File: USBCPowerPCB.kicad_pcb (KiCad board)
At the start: 4 copper layers, 101 parts, among them IC2 TPS56A37RPAR, J1 USB_C_Receptacle_PowerOnly_6P, J10 GND_BANANA_OUT, J2 CC, J3 12V_OUT, J4 5V_ISOOUT, J5 5V_UNISOOUT, J6 12V_OUT_PIN, J7 5V_ISOOUT_PIN, J8 5V_UNISOOUT_PIN, J9 12V_BANANA_OUT, Q1 IRF9358TRPBF, Q2 BSL308PEH6327XTSA1, U1 TVS2200DRV, U2 CYPD3177-24LQXQT, U3 TPS562231DRLR, U4 TPS2116DRL, U5 TBA2-2411

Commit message: started routing
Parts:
- C11, C19, C9: footprint Capacitor_SMD:C_2220_5750Metric -> Capacitor_SMD:C_0805_2012Metric
- C14, NT1, R21, R23: moved to B.Cu
- C17, C18, C21, C22: footprint Capacitor_SMD:C_1210_3225Metric -> Capacitor_SMD:C_0805_2012Metric
- TP1, TP10, TP11, TP12, TP13, TP2, TP3, TP4, TP5, TP6, TP7, TP8, TP9: footprint TestPoint:TestPoint_Pad_D2.5mm -> TestPoint:TestPoint_Plated_Hole_D3.0mm
- moved J9 174.6 mm to (276.2, 113.1), turned to -90 degrees
- moved J10 154.3 mm to (259.9, 113.1), turned to -90 degrees
- moved L1 121.6 mm to (256.5, 100.5)
- moved C18 115.1 mm to (262.2, 107.8), turned to -90 degrees
- moved C9 111.8 mm to (243.0, 101.0), turned to -90 degrees
- moved C17 111.6 mm to (259.2, 107.8), turned to -90 degrees
- moved R24 111.3 mm to (248.6, 105.9), turned to 90 degrees
- moved C11 110.3 mm to (240.2, 101.0), turned to -90 degrees
- moved D9 108.9 mm to (237.5, 109.6), turned to 90 degrees
- moved C15 108.8 mm to (248.5, 96.8), turned to 90 degrees
- moved R25 106.2 mm to (242.9, 105.9), turned to -90 degrees
- moved C16 104.7 mm to (245.7, 106.0), turned to 90 degrees
- moved R23 104.4 mm to (242.9, 113.7), turned to -90 degrees
- moved R21 104.3 mm to (242.9, 110.0), turned to -90 degrees
- moved C14 103.0 mm to (245.6, 110.0), turned to -90 degrees
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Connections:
- net Net-(IC2-SW) renamed /12V Buck Converter/SW
- J4 pad 2: GNDPWR -> unconnected-(J4-Pin_2-Pad2)
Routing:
- net Net-(IC2-EN): track 0.00 -> 16.4 mm, vias 0 -> 1
- net Net-(IC2-MODE): track 0.00 -> 10.3 mm, vias 0 -> 1
- net GND: track 0.00 -> 8.94 mm, vias 0 -> 5
- net Net-(IC2-SS): track 0.00 -> 8.67 mm, vias 0 -> 1
- net /12V Buck Converter/FB: track 0.00 -> 8.16 mm
- net /VBUS: track 0.00 -> 6.09 mm
- net /12V Buck Converter/POWER_GOOD: track 0.00 -> 1.90 mm
- net GNDA: track 0.00 -> 1.17 mm, vias 0 -> 1
- added copper zone on F.Cu, net +12V
- added copper zone on F.Cu, net /12V Buck Converter/SW
- added copper zone on In2.Cu, net /VBUS
- added copper zone on B.Cu, net GND
- added copper zone on In1.Cu, net GND
- added copper zone on B.Cu, net GNDA
- added copper zone on In1.Cu, net GNDA

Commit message: more layout updates
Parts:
- moved C9 233.1 mm to (18.6, 38.1)
- moved C11 227.9 mm to (21.2, 38.1)
- moved C14 227.9 mm to (26.6, 47.0)
- moved C15 227.9 mm to (29.5, 33.9)
- moved C16 227.9 mm to (26.7, 43.0)
- moved C17 227.9 mm to (40.2, 44.9)
- moved C18 227.9 mm to (43.2, 44.9)
- moved D9 227.9 mm to (18.5, 46.7)
- moved IC2 227.9 mm to (28.1, 38.5)
- moved L1 227.9 mm to (37.5, 37.6)
- moved NT1 227.9 mm to (26.6, 52.1)
- moved R21 227.9 mm to (23.9, 47.0)
- moved R22 227.9 mm to (21.2, 43.0)
- moved R23 227.9 mm to (23.9, 50.7)
- moved R24 227.9 mm to (29.6, 43.0)
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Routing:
- net /12V Buck Converter/POWER_GOOD: track 1.90 -> 15.1 mm, vias 0 -> 2
- net GND: track 8.94 -> 18.9 mm, vias 5 -> 12
- net Net-(IC2-BOOT): track 0.00 -> 2.78 mm
- net Net-(IC2-MODE): track 10.3 -> 7.89 mm
- net Net-(IC2-EN): track 16.4 -> 16.9 mm, vias 1 -> 2
- added copper zone on In2.Cu, net +12V
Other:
- board outline added: 100 x 100 mm

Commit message: redid cypd layout, halfway through 12v buck layout
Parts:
- removed C10: 0.1uF, Capacitor_SMD:C_0805_2012Metric
- removed C13: 22uF, Capacitor_SMD:C_1210_3225Metric
- C14, NT1, R21, R23: moved to F.Cu
- J4: footprint UTSVT_Connectors:Molex_MicroFit3.0_1x2xP3.00mm_PolarizingPeg_Vertical -> UTSVT_Connectors:Molex_MicroFit3.0_1x4xP3.00mm_PolarizingPeg_Vertical
- L2: footprint UTSVT_Passive:INDPM110100X400N -> UTSVT_Passive:INDPM5452X300N
- R11, R13, R15, R17, R19, R20, R8: moved to B.Cu
- TP10, TP11, TP12, TP13: footprint TestPoint:TestPoint_Plated_Hole_D3.0mm -> TestPoint:TestPoint_THTPad_1.0x1.0mm_Drill0.5mm
- moved TP4 230.7 mm to (243.4, 90.1)
- moved J3 200.1 mm to (251.9, 60.2), turned to 0 degrees
- moved J6 198.7 mm to (249.1, 73.5), turned to 0 degrees
- moved TP1 177.7 mm to (237.3, 90.1)
- moved C9 140.4 mm to (130.5, 122.9), turned to 0 degrees
- moved R1 138.8 mm to (254.7, 88.5)
- moved R2 138.8 mm to (254.7, 91.5)
- moved R3 138.8 mm to (254.7, 94.4)
- moved R4 138.8 mm to (254.7, 97.4)
- moved R5 138.8 mm to (254.7, 100.3)
- moved R6 138.8 mm to (254.7, 103.3)
- moved C11 136.9 mm to (130.5, 120.6), turned to 0 degrees
- moved C12 133.3 mm to (130.5, 118.3), turned to 0 degrees
- moved R21 132.3 mm to (136.8, 116.0), turned to 0 degrees
- moved IC2 129.1 mm to (132.4, 114.6), turned to 180 degrees
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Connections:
- net Net-(U3-SW) renamed /5V Buck Converter/SW
- R26 pad 1: +3.3V -> +12V
- R31 pad 1: +5V -> /5V_BUCK
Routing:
- net /CC2: track 0.00 -> 26.3 mm, vias 0 -> 2
- net /CC1: track 0.00 -> 22.6 mm
- net /Power Delivery Controller/VBUS_MAX: track 0.00 -> 17.7 mm, vias 0 -> 1
- net /Power Delivery Controller/ISNK_COARSE: track 0.00 -> 17.3 mm, vias 0 -> 1
- net Net-(IC2-EN): track 16.9 -> 0.00 mm, vias 2 -> 0
- net /Power Delivery Controller/VBUS_MIN: track 0.00 -> 15.4 mm, vias 0 -> 1
- net Net-(Q1A-G): track 0.00 -> 15.2 mm
- net /12V Buck Converter/POWER_GOOD: track 15.1 -> 0.00 mm, vias 2 -> 0
- net /Power Delivery Controller/ISNK_FINE: track 0.00 -> 15.0 mm, vias 0 -> 1
- net GND: track 18.9 -> 31.8 mm, vias 12 -> 22
- net Net-(IC2-SS): track 8.67 -> 0.00 mm, vias 1 -> 0
- net /12V Buck Converter/FB: track 8.08 -> 0.00 mm
- net Net-(IC2-MODE): track 7.89 -> 0.00 mm, vias 1 -> 0
- net /VBUS: track 6.09 -> 0.00 mm
- net Net-(Q2A-G): track 0.00 -> 5.68 mm
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- added copper zone on F.Cu, net +3.3V
- added copper zone on F.Cu, net /SAFE_5V
- added copper zone on F.Cu, net /VBUS_USBIN
- removed copper zone on F.Cu, net +12V
- removed copper zone on In2.Cu, net +12V
- removed copper zone on F.Cu, net /12V Buck Converter/SW
- removed copper zone on In2.Cu, net /VBUS
- removed copper zone on In1.Cu, net GND
- removed copper zone on B.Cu, net GNDA
- removed copper zone on In1.Cu, net GNDA
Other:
- board size 100 x 100 mm -> 99.8 x 100 mm
- copper layers 4 -> 2

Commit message: big component layout moment
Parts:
- added TP14: 12V_UVLO, TestPoint:TestPoint_THTPad_1.0x1.0mm_Drill0.5mm, F.Cu at (235.7, 113.1)
- added TP15: 5V_SET, TestPoint:TestPoint_THTPad_1.0x1.0mm_Drill0.5mm, F.Cu at (235.7, 120.0)
- added TP16: 12V_SET, TestPoint:TestPoint_THTPad_1.0x1.0mm_Drill0.5mm, F.Cu at (235.7, 116.2)
- NT1, R30, R31: moved to B.Cu
- TP1, TP2, TP3, TP4, TP5, TP6, TP7, TP8, TP9: footprint TestPoint:TestPoint_Plated_Hole_D3.0mm -> TestPoint:TestPoint_Plated_Hole_D2.0mm
- moved U3 131.6 mm to (149.6, 109.8), turned to 90 degrees
- moved L2 131.3 mm to (151.8, 114.5)
- moved C19 129.5 mm to (146.5, 110.4), turned to 180 degrees
- moved R28 127.8 mm to (147.7, 107.1), turned to 180 degrees
- moved R27 126.3 mm to (149.5, 104.9), turned to 180 degrees
- moved C20 122.6 mm to (151.3, 107.1)
- moved R29 120.2 mm to (154.3, 122.1), turned to 180 degrees
- moved R31 119.9 mm to (154.5, 127.9)
- moved R30 119.9 mm to (154.3, 122.1)
- moved U4 119.3 mm to (154.2, 125.3), turned to -90 degrees
- moved C21 118.4 mm to (155.1, 108.0)
- moved C22 118.1 mm to (155.1, 110.2)
- moved F1 109.8 mm to (165.3, 104.8), turned to 90 degrees
- moved U5 107.6 mm to (162.7, 124.6), turned to 180 degrees
- moved R22 48.5 mm to (141.2, 119.3), turned to 180 degrees
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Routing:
- net /5V_BUCK: track 0.00 -> 27.4 mm, vias 0 -> 1
- net GND: track 31.8 -> 58.5 mm, vias 22 -> 41
- net /12V Buck Converter/FB: track 0.00 -> 12.9 mm
- net GNDA: track 0.00 -> 10.9 mm, vias 0 -> 8
- net /12V Buck Converter/POWER_GOOD: track 0.00 -> 10.4 mm
- net Net-(IC2-EN): track 0.00 -> 10.4 mm
- net /Power Delivery Controller/VBUS_MIN: track 15.4 -> 7.30 mm, vias 1 -> 0
- net /Power Delivery Controller/VBUS_MAX: track 17.7 -> 9.76 mm, vias 1 -> 0
- net /Power Delivery Controller/ISNK_FINE: track 15.0 -> 7.29 mm, vias 1 -> 0
- net /Power Delivery Controller/ISNK_COARSE: track 17.3 -> 9.75 mm, vias 1 -> 0
- net /5V Buck Converter/SW: track 0.00 -> 6.83 mm, vias 0 -> 2
- net Net-(U5-+Vout): track 0.00 -> 6.81 mm
- net +3.3V: track 0.00 -> 4.97 mm
- net /5V ORring and Isolator/MUX_SEL: track 0.00 -> 4.66 mm, vias 0 -> 1
- net Net-(U3-FB): track 0.00 -> 4.31 mm
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- added copper zone on F.Cu, net +12V
- added copper zone on F.Cu, net +5V
- added copper zone on F.Cu, net /12V Buck Converter/SW
- added copper zone on F.Cu, net /5V Buck Converter/SW
- added copper zone on F.Cu, net /5V_BUCK
- added copper zone on F.Cu, net /5V_ISOOUT
- added copper zone on B.Cu, net GNDA
- added copper zone on B.Cu, net GNDPWR
- added copper zone on F.Cu, net Net-(IC2-BOOT)
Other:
- board text added: "PG"

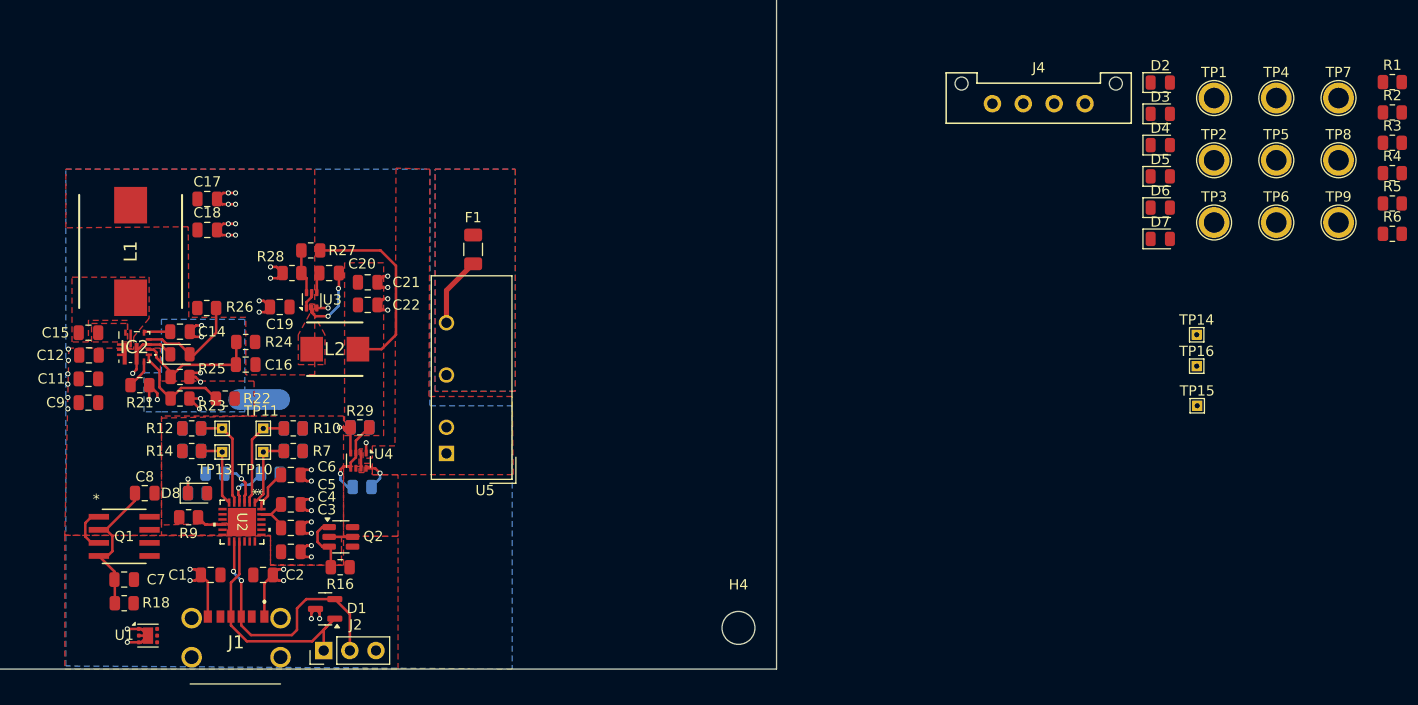
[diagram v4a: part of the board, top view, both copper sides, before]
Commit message: added testpoints everywhere :)
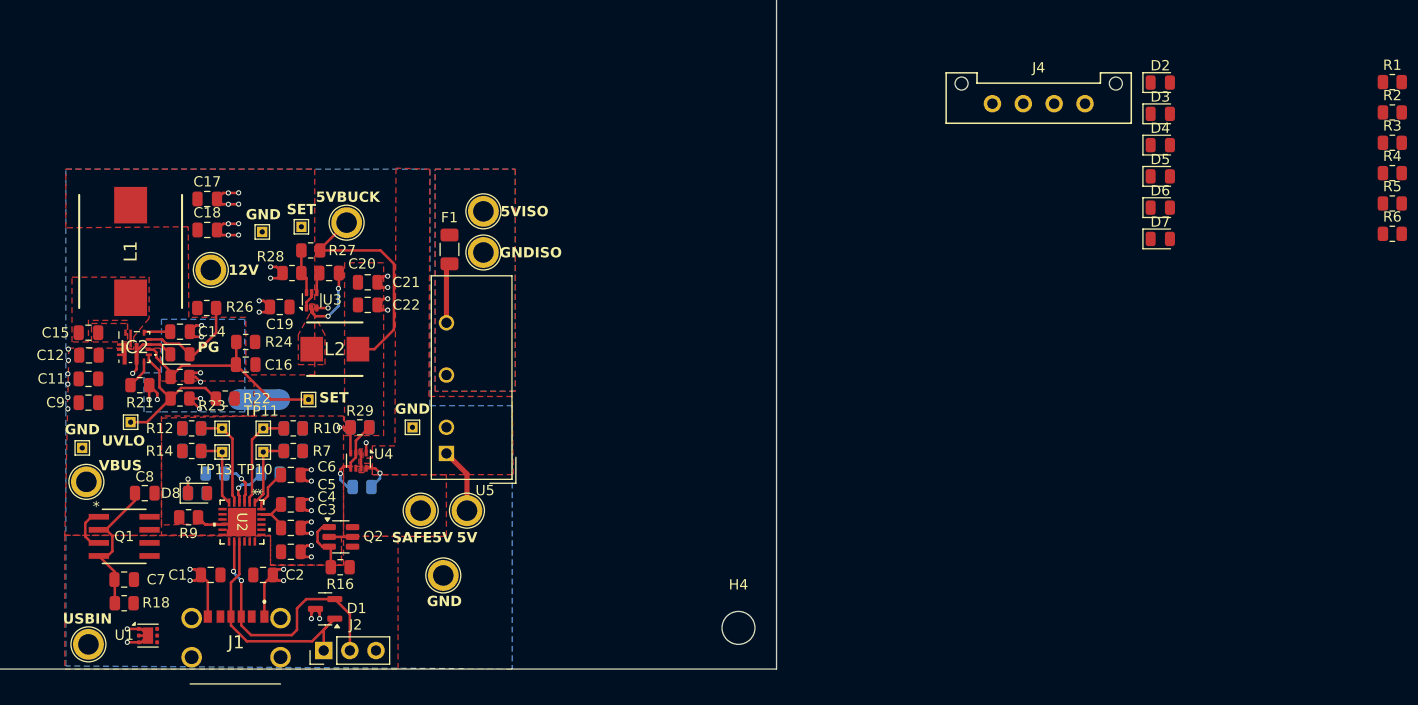
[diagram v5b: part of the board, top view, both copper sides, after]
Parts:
- added TP17: GND_TP, TestPoint:TestPoint_THTPad_1.0x1.0mm_Drill0.5mm, F.Cu at (159.4, 122.1)
- added TP18: GND_TP, TestPoint:TestPoint_THTPad_1.0x1.0mm_Drill0.5mm, F.Cu at (127.3, 124.1)
- added TP19: GND_TP, TestPoint:TestPoint_Plated_Hole_D2.0mm, F.Cu at (162.4, 136.5)
- J4: value 5V_ISOOUT -> 5V_ISO
- J5: value 5V_UNISOOUT -> 5V_OUT
- J7: value 5V_ISOOUT_PIN -> 5V_ISO_PIN
- J8: value 5V_UNISOOUT_PIN -> 5V_OUT_PIN
- TP1: value 12V_OUT_TP -> 12V_TP
- TP2: value 5V_UNISO_TP -> 5V_TP
- TP5: footprint TestPoint:TestPoint_Plated_Hole_D2.0mm -> TestPoint:TestPoint_THTPad_1.0x1.0mm_Drill0.5mm
- TP6: value 5V_ISOOUT_TP -> 5V_ISO_TP
- moved TP4 121.6 mm to (127.7, 127.4)
- moved TP3 116.9 mm to (127.9, 143.2)
- moved TP14 104.0 mm to (132.0, 121.6)
- moved TP1 99.0 mm to (139.8, 106.8)
- moved TP5 98.8 mm to (144.8, 103.1)
- moved TP7 97.8 mm to (160.2, 130.2)
- moved TP9 96.4 mm to (153.0, 102.2)
- moved TP15 88.8 mm to (148.6, 102.6)
- moved TP16 86.4 mm to (149.3, 119.4)
- moved TP8 83.6 mm to (166.3, 105.1)
- moved TP2 80.2 mm to (164.7, 130.2)
- moved TP6 77.1 mm to (166.3, 101.1)
- moved F1 2.30 mm to (163.0, 104.8)
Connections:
- net /5V_ISOOUT renamed /5V_ISO
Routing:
- net /12V Buck Converter/FB: track 12.9 -> 21.4 mm
- net +5V: track 1.48 -> 7.87 mm
- net Net-(IC2-EN): track 10.4 -> 15.2 mm
- net /5V_BUCK: track 27.4 -> 30.6 mm
- net GND: track 58.5 -> 59.7 mm
- net Net-(U5-+Vout): track 6.81 -> 5.86 mm
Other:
- board text added: "12V"
- board text added: "5V"
- board text added: "5VBUCK"
- board text added: "5VISO"
- board text added: "GND"
- board text added: "GNDISO"
- board text added: "SAFE5V"
- board text added: "SET"
- board text added: "USBIN"
- board text added: "UVLO"
- board text added: "VBUS"

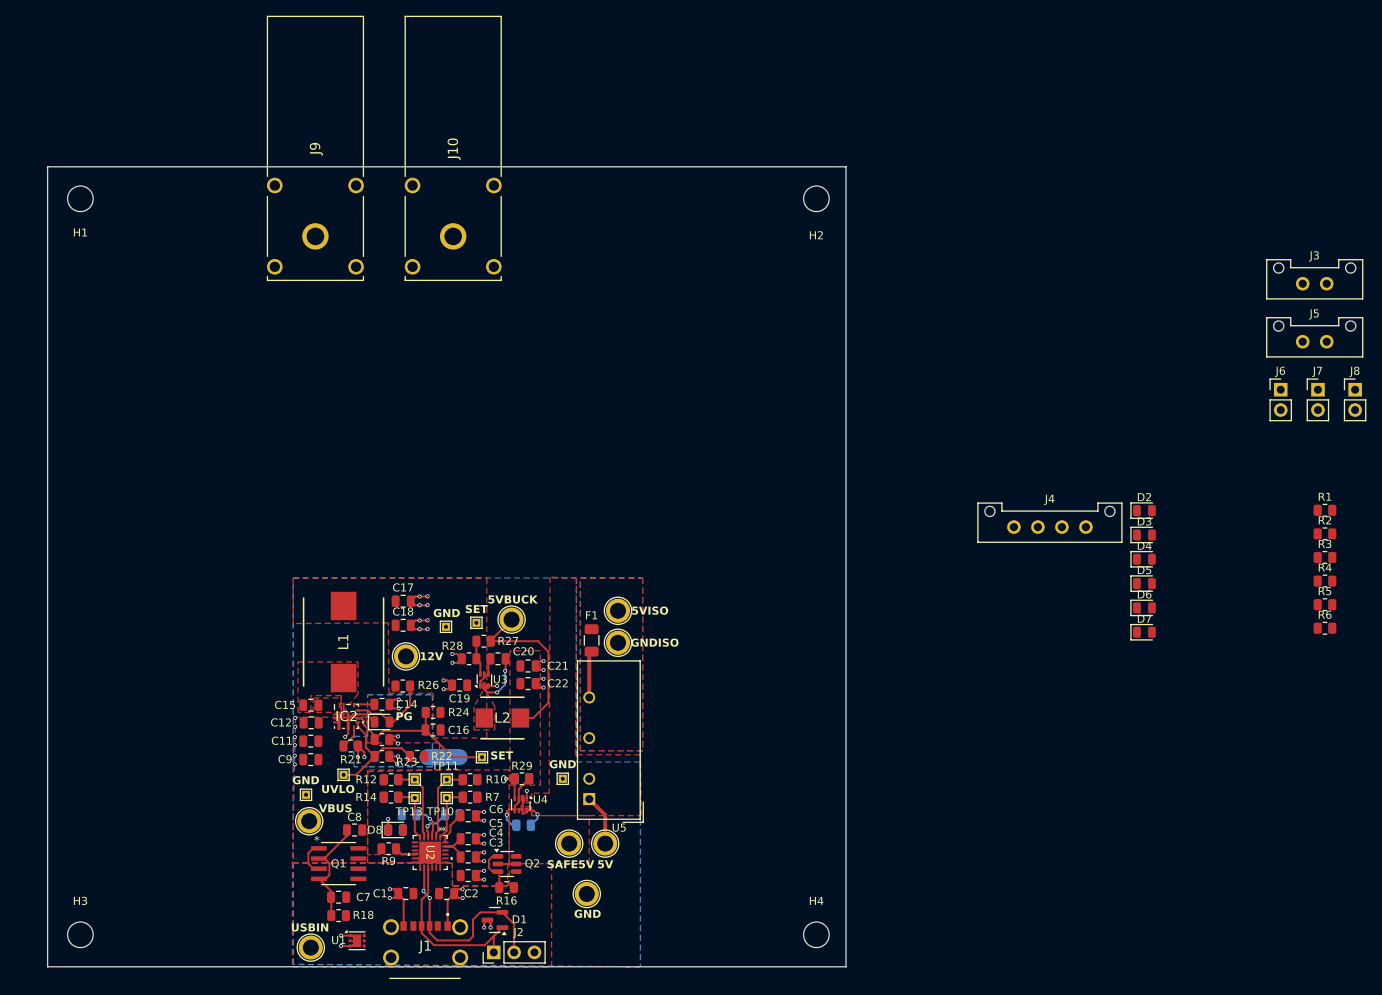
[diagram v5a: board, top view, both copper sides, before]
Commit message: cleared most DRC errors, need to fix DRC warnings
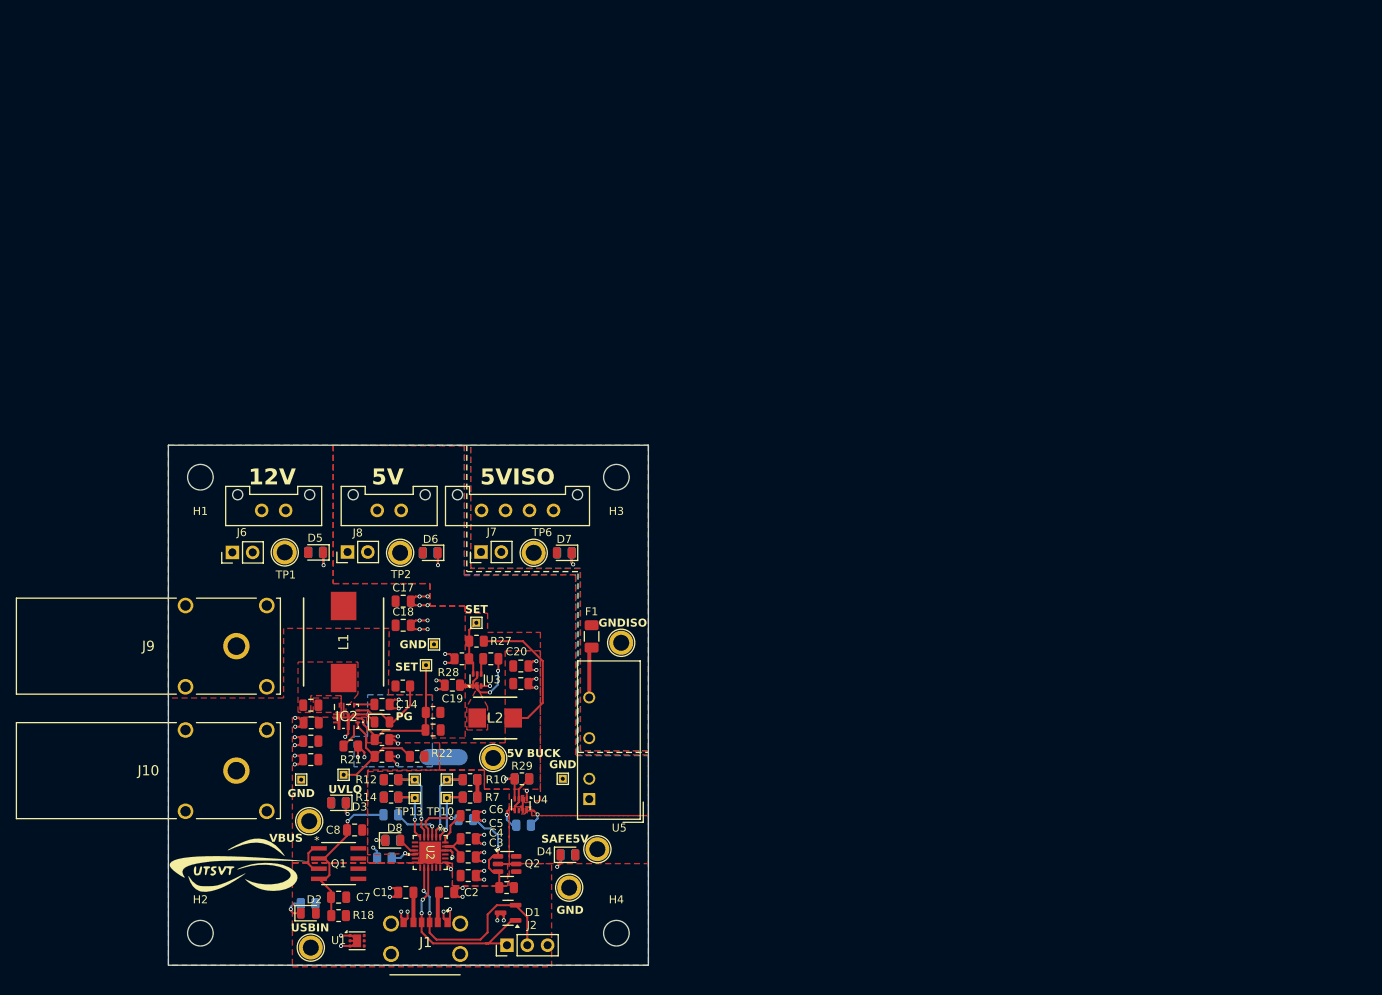
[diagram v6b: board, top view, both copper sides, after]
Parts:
- added G***: LOGO, UTSVT_Special:UTSVT_Logo_Symbol, F.Cu at (118.7, 133.0)
- R1, R2, R3, R4, R5, R6, R9: moved to B.Cu
- moved R1 136.3 mm to (127.6, 137.7), turned to 180 degrees
- moved J3 133.2 mm to (121.8, 88.5)
- moved J6 132.6 mm to (118.1, 93.8), turned to 90 degrees
- moved R2 127.8 mm to (131.4, 125.1)
- moved J8 127.6 mm to (132.5, 93.8), turned to 90 degrees
- moved R4 126.2 mm to (128.5, 93.8)
- moved H2 119.8 mm to (114.1, 141.4)
- moved J5 117.6 mm to (136.2, 88.5)
- moved D2 116.0 mm to (127.6, 138.9)
- moved R5 112.0 mm to (142.8, 93.8)
- moved J7 106.6 mm to (149.2, 93.8), turned to 90 degrees
- moved D3 106.2 mm to (131.4, 125.1), turned to 180 degrees
- moved D5 103.7 mm to (128.5, 93.8), turned to 180 degrees
- moved R3 101.7 mm to (160.0, 131.6), turned to 180 degrees
- moved R6 95.5 mm to (159.6, 93.8)
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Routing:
- net GND: track 59.7 -> 69.7 mm, vias 41 -> 47
- net /VBUS_USBIN: track 0.00 -> 7.56 mm
- net Net-(Q2A-G): track 5.68 -> 12.2 mm, vias 0 -> 1
- net +5V: track 7.87 -> 1.48 mm
- net Net-(Q1A-G): track 15.2 -> 21.2 mm, vias 0 -> 1
- net /5V_BUCK: track 30.6 -> 26.5 mm
- net +3.3V: track 4.97 -> 8.67 mm, vias 0 -> 1
- net Net-(D4-K): track 0.00 -> 3.34 mm, vias 0 -> 1
- net Net-(D2-K): track 0.00 -> 3.30 mm, vias 0 -> 1
- net Net-(D5-K): track 0.00 -> 3.26 mm, vias 0 -> 1
- net Net-(D6-K): track 0.00 -> 3.14 mm, vias 0 -> 1
- net Net-(D7-K): track 0.00 -> 3.06 mm, vias 0 -> 1
- net Net-(D3-K): track 0.00 -> 2.98 mm, vias 0 -> 1
- net Net-(U3-FB): track 4.31 -> 6.98 mm
- net /12V Buck Converter/FB: track 21.4 -> 18.8 mm
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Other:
- board size 99.8 x 100 mm -> 60 x 65 mm
- board text added: "5V BUCK"
- board text removed: "5VBUCK"
